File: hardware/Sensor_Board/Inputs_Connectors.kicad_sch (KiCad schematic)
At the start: 0 parts

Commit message: feat(Hw):Batt_Board_Pro_Added
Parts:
- added FLEX1: FH12-24S-0.5SH(55), Connector_FFC-FPC:Hirose_FH12-24S-0.5SH_1x24-1MP_P0.50mm_Horizontal, symbol F31L-1A7H1-11024:F31L-1A7H1-11024
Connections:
- new net +3.3V: FLEX1.1, FLEX1.2
- new net AP_ADO: FLEX1.16
- new net DIO2: FLEX1.3
- new net FSYNC: FLEX1.18
- new net GND: FLEX1.24
- new net INT1: FLEX1.17
- new net INT2: FLEX1.19
- new net R0_ANT_SW: FLEX1.13
- new net R0_BUSY: FLEX1.9
- new net R0_DIO1: FLEX1.12
- new net R0_DIO2: FLEX1.11
- new net R0_DIO3: FLEX1.10
- new net R0_MISO: FLEX1.6
- new net R0_MOSI: FLEX1.7
- new net R0_NSS: FLEX1.4
- new net R0_RST: FLEX1.8
- new net R0_SCK: FLEX1.5
- new net SCL_BME280: FLEX1.21, FLEX1.23
- new net SCL_ICM: FLEX1.15
- new net SDA_BME280: FLEX1.20, FLEX1.22
- new net SDA_ICM: FLEX1.14

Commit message: feat(Hw):Update_Battery_Sch_And_Sensors_And_PWNCube
pending_Outputs_connectors
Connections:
- net +3.3V: no longer FLEX1.2
- net SCL_BME280: no longer FLEX1.23
- net SDA_BME280: no longer FLEX1.22
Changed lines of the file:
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@@
 	(generator_version "9.0")
 	(paper "A4")
-	(junction
-		(at 115.57 52.07)
-		(diameter 0)
-		(color 0 0 0 0)
-	)
 	(wire
 		(pts
@@
 	(wire
 		(pts
-			(xy 115.57 52.07) (xy 111.76 52.07)
+			(xy 111.76 52.07) (xy 119.38 52.07)
 		)
 		(stroke
@@
 	(wire
 		(pts
-			(xy 115.57 48.26) (xy 115.57 52.07)
-		)
-		(stroke
-			(width 0)
-			(type default)
-		)
-	)
-	(wire
-		(pts
 			(xy 114.3 82.55) (xy 119.38 82.55)
 		)
@@
 	(wire
 		(pts
-			(xy 115.57 52.07) (xy 119.38 52.07)
-		)
-		(stroke
-			(width 0)
-			(type default)
-		)
-	)
-	(wire
-		(pts
 			(xy 119.38 110.49) (xy 113.03 110.49)
 		)
@@
 	(wire
 		(pts
-			(xy 115.57 54.61) (xy 115.57 52.07)
-		)
-		(stroke
-			(width 0)
-			(type default)
-		)
-	)
-	(wire
-		(pts
 			(xy 114.3 90.17) (xy 119.38 90.17)
 		)
@@
 		)
 	)
+	(hierarchical_label "R1_SCK"
+		(shape input)
+		(at 63.5 135.89 180)
+		(effects
+			(font
+				(size 1.27 1.27)
+			)
+			(justify right)
+		)
+	)
+	(hierarchical_label "R1_DIO1"
+		(shape input)
+		(at 63.5 153.67 180)
+		(effects
+			(font
+				(size 1.27 1.27)
+			)
+			(justify right)
+		)
+	)
+	(hierarchical_label "R1_MISO"
+		(shape input)
+		(at 63.5 138.43 180)
+		(effects
+			(font
+				(size 1.27 1.27)
+			)
+			(justify right)
+		)
+	)
+	(hierarchical_label "+3.3V"
+		(shape output)
+		(at 111.76 52.07 180)
+		(effects
+			(font
+				(size 1.27 1.27)
+			)
+			(justify right)
+		)
+	)
+	(hierarchical_label "INT2"
+		(shape input)
+		(at 114.3 97.79 180)
+		(effects
+			(font
+				(size 1.27 1.27)
+			)
+			(justify right)
+		)
+	)
 	(hierarchical_label "SCL_BME280"
 		(shape output)
-		(at 114.3 107.95 180)
-		(effects
-			(font
-				(size 1.27 1.27)
-			)
-			(justify right)
-		)
-	)
-	(hierarchical_label "R1_SCK"
-		(shape input)
-		(at 63.5 135.89 180)
-		(effects
-			(font
-				(size 1.27 1.27)
-			)
-			(justify right)
-		)
-	)
-	(hierarchical_label "R1_DIO1"
-		(shape input)
-		(at 63.5 153.67 180)
-		(effects
-			(font
-				(size 1.27 1.27)
-			)
-			(justify right)
-		)
-	)
-	(hierarchical_label "R1_MISO"
-		(shape input)
-		(at 63.5 138.43 180)
-		(effects
-			(font
-				(size 1.27 1.27)
-			)
-			(justify right)
-		)
-	)
-	(hierarchical_label "+3.3V"
-		(shape output)
-		(at 111.76 52.07 180)
-		(effects
-			(font
-				(size 1.27 1.27)
-			)
-			(justify right)
-		)
-	)
-	(hierarchical_label "INT2"
-		(shape input)
-		(at 114.3 97.79 180)
-		(effects
-			(font
-				(size 1.27 1.27)
-			)
-			(justify right)
-		)
-	)
-	(hierarchical_label "SCL_BME280"
-		(shape output)
 		(at 114.3 102.87 180)
 		(effects
@@
 		(shape output)
 		(at 114.3 95.25 180)
-		(effects
-			(font
-				(size 1.27 1.27)
-			)
-			(justify right)
-		)
-	)
-	(hierarchical_label "SDA_BME280"
-		(shape bidirectional)
-		(at 114.3 105.41 180)
 		(effects
 			(font
@@
 					(unit 1)
 				)
-			)
-		)
-	)
-	(symbol
-		(lib_id "power:+3.3V")
-		(at 115.57 48.26 0)
-		(unit 1)
-		(exclude_from_sim no)
-		(in_bom yes)
-		(on_board yes)
-		(dnp no)
-		(fields_autoplaced yes)
-		(property "Reference" "#PWR064"
-			(at 115.57 52.07 0)
-			(effects
-				(font
-					(size 1.27 1.27)
-				)
-				(hide yes)
-			)
-		)
-		(property "Value" "+3.3V"
-			(at 115.57 43.18 0)
-			(effects
-				(font
-					(size 1.27 1.27)
-				)
-			)
-		)
-		(property "Footprint" ""
-			(at 115.57 48.26 0)
-			(effects
-				(font
-					(size 1.27 1.27)
-				)
-				(hide yes)
-			)
-		)
-		(property "Datasheet" ""
-			(at 115.57 48.26 0)
-			(effects
-				(font
-					(size 1.27 1.27)
-				)
-				(hide yes)
-			)
-		)
-		(property "Description" "Power symbol creates a global label with name \"+3.3V\""
-			(at 115.57 48.26 0)
-			(effects
-				(font
-					(size 1.27 1.27)
-				)
-				(hide yes)
-			)
-		)
-		(pin "1"
-		)
-		(instances
-			(project "Sensor_Board"
-				(path "/671dafcd-6579-4545-95ba-aa32d81f1541/082363ca-5881-4851-9449-c4a5f2b44a24"
-					(reference "#PWR064")
-					(unit 1)
-				)

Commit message: feat(Hw):floorplans_updated
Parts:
- removed FLEX1: FH12-24S-0.5SH(55), Connector_FFC-FPC:Hirose_FH12-24S-0.5SH_1x24-1MP_P0.50mm_Horizontal, symbol F31L-1A7H1-11024:F31L-1A7H1-11024
- added J3: Sensors, Connector_PinHeader_2.54mm:PinHeader_2x20_P2.54mm_Vertical, symbol Connector_Generic:Conn_02x20_Odd_Even
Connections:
- net +3.3V: now also J3.2 (Pin_2), J3.4 (Pin_4), J3.6 (Pin_6)
- net AP_ADO: now also J3.12 (Pin_12)
- net DIO2: now also J3.1 (Pin_1)
- net DIO23: now also J3.25 (Pin_25)
- net FSYNC: now also J3.16 (Pin_16)
- net GND: now also J3.36 (Pin_36), J3.38 (Pin_38), J3.40 (Pin_40)
- net INT1: now also J3.14 (Pin_14)
- net INT2: now also J3.18 (Pin_18)
- net R0_ANT_SW: now also J3.21 (Pin_21)
- net R0_BUSY: now also J3.13 (Pin_13)
- net R0_DIO1: now also J3.19 (Pin_19)
- net R0_DIO2: now also J3.17 (Pin_17)
- net R0_DIO3: now also J3.15 (Pin_15)
- net R0_MISO: now also J3.7 (Pin_7)
- net R0_MOSI: now also J3.9 (Pin_9)
- net R0_NSS: now also J3.3 (Pin_3)
- net R0_RST: now also J3.11 (Pin_11)
- net R0_SCK: now also J3.5 (Pin_5)
- net R1_ANT_SW: now also J3.23 (Pin_23)
- net R1_BUSY: now also J3.37 (Pin_37)
- net R1_DIO1: now also J3.32 (Pin_32)
- net R1_DIO2: now also J3.34 (Pin_34)
- net R1_DIO3: now also J3.39 (Pin_39)
- net R1_MISO: now also J3.31 (Pin_31)
- net R1_MOSI: now also J3.33 (Pin_33)
- net R1_NSS: now also J3.27 (Pin_27)
- net R1_RST: now also J3.35 (Pin_35)
- net R1_SCK: now also J3.29 (Pin_29)
- net SCL_BME280: now also J3.22 (Pin_22)
- net SCL_ICM: now also J3.10 (Pin_10)
- net SDA_BME280: now also J3.20 (Pin_20)
- net SDA_ICM: now also J3.8 (Pin_8)
- no-connect marks 0 -> 4

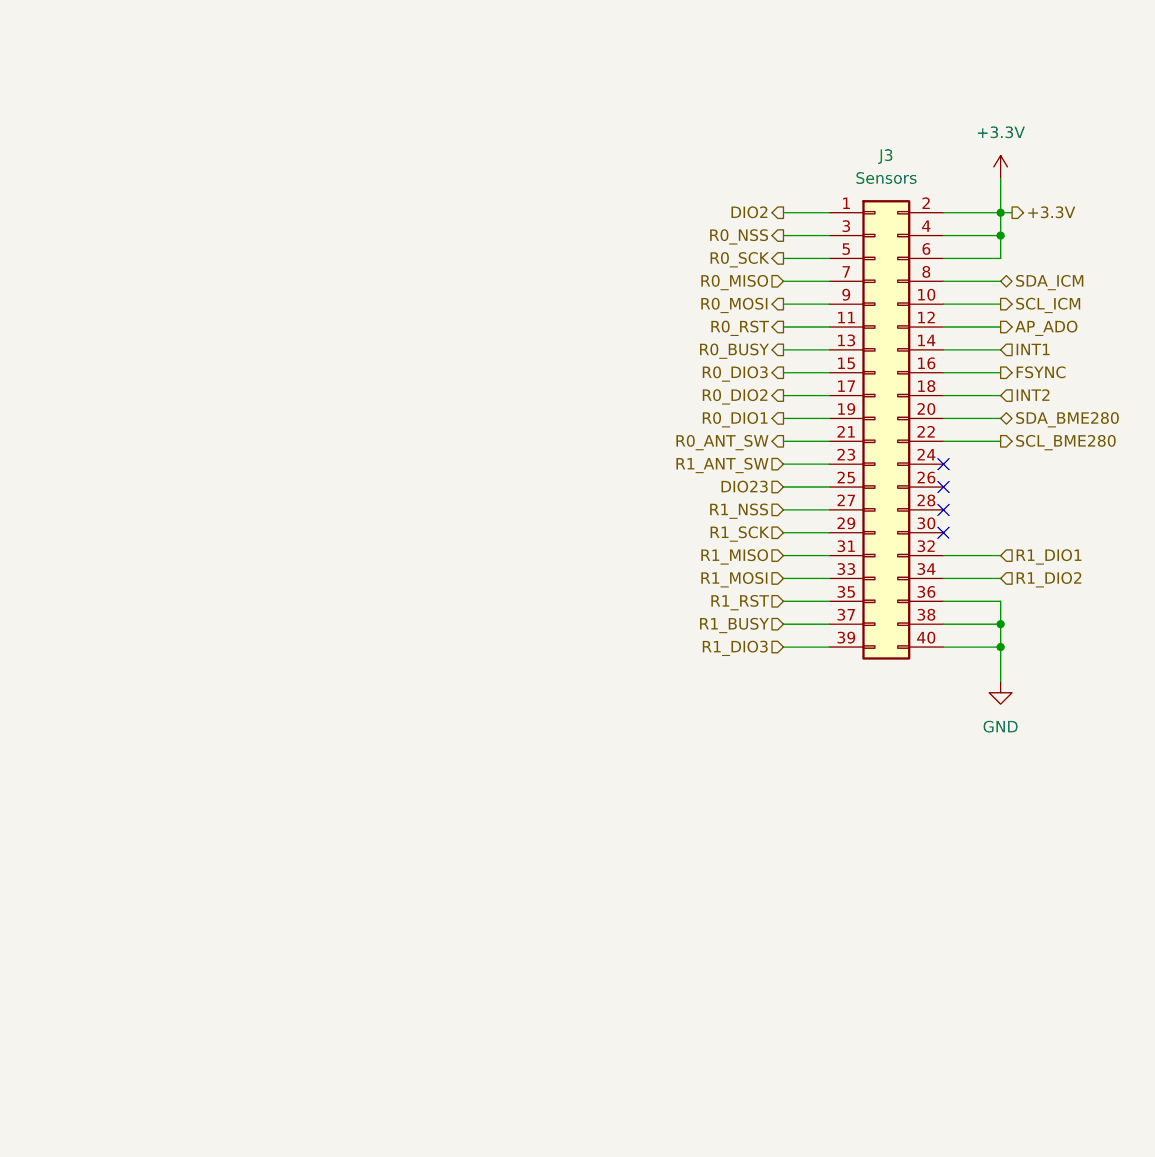
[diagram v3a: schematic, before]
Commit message: feat(Hw):Update_Route_And_3d_Model_PWNsat_Batt_Board_And_Sensors
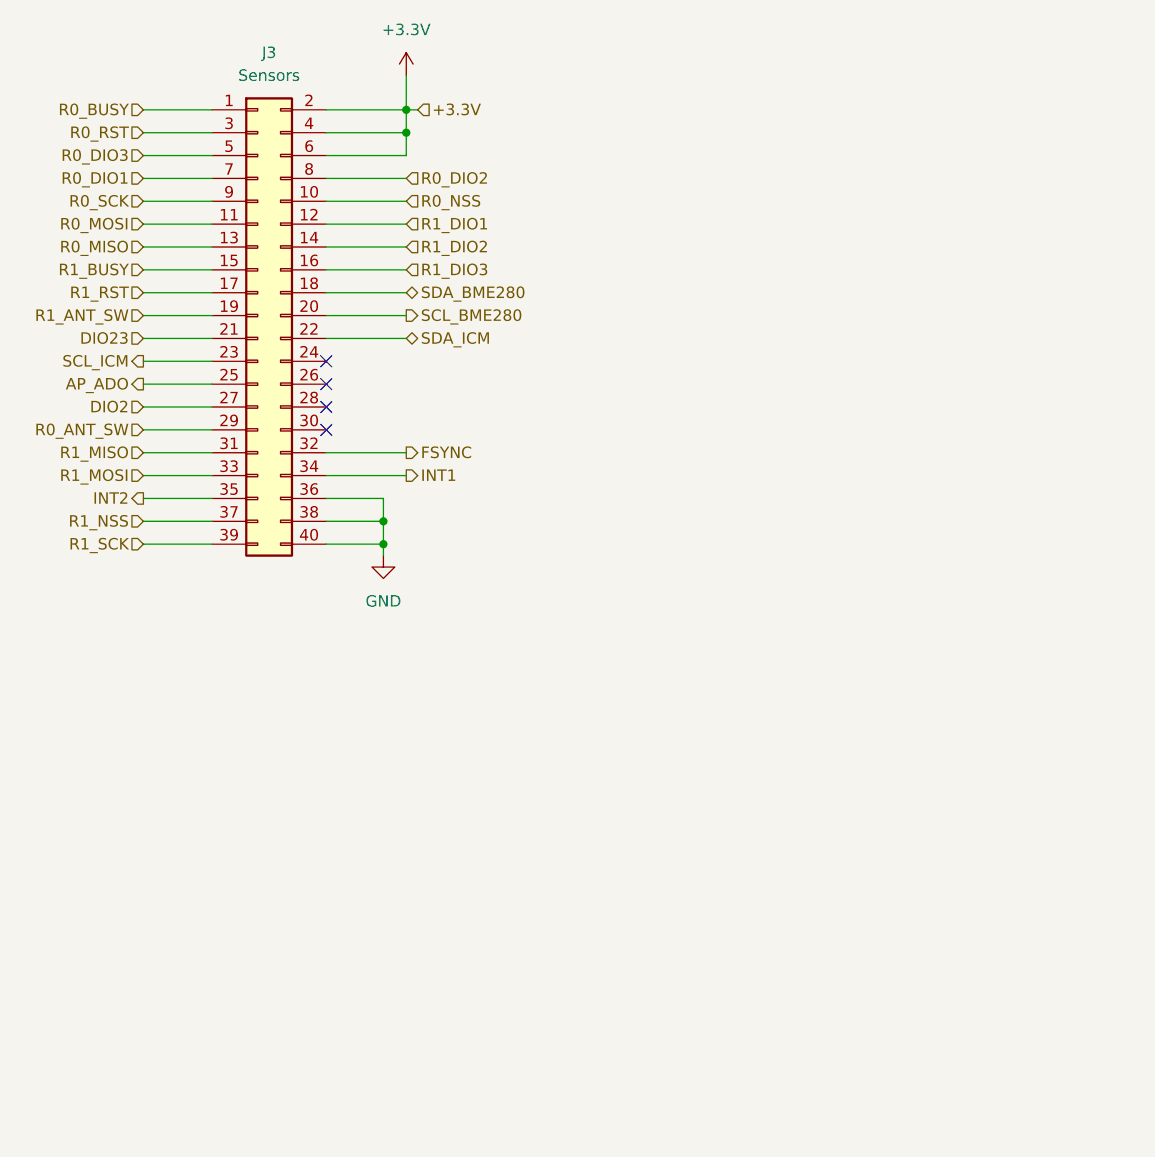
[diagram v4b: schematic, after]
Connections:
- net AP_ADO: now also J3.25 (Pin_25); no longer J3.12 (Pin_12)
- net DIO2: now also J3.27 (Pin_27); no longer J3.1 (Pin_1)
- net DIO23: now also J3.21 (Pin_21); no longer J3.25 (Pin_25)
- net FSYNC: now also J3.32 (Pin_32); no longer J3.16 (Pin_16)
- net INT1: now also J3.34 (Pin_34); no longer J3.14 (Pin_14)
- net INT2: now also J3.35 (Pin_35); no longer J3.18 (Pin_18)
- net R0_ANT_SW: now also J3.29 (Pin_29); no longer J3.21 (Pin_21)
- net R0_BUSY: now also J3.1 (Pin_1); no longer J3.13 (Pin_13)
- net R0_DIO1: now also J3.7 (Pin_7); no longer J3.19 (Pin_19)
- net R0_DIO2: now also J3.8 (Pin_8); no longer J3.17 (Pin_17)
- net R0_DIO3: now also J3.5 (Pin_5); no longer J3.15 (Pin_15)
- net R0_MISO: now also J3.13 (Pin_13); no longer J3.7 (Pin_7)
- net R0_MOSI: now also J3.11 (Pin_11); no longer J3.9 (Pin_9)
- net R0_NSS: now also J3.10 (Pin_10); no longer J3.3 (Pin_3)
- net R0_RST: now also J3.3 (Pin_3); no longer J3.11 (Pin_11)
- net R0_SCK: now also J3.9 (Pin_9); no longer J3.5 (Pin_5)
- net R1_ANT_SW: now also J3.19 (Pin_19); no longer J3.23 (Pin_23)
- net R1_BUSY: now also J3.15 (Pin_15); no longer J3.37 (Pin_37)
- net R1_DIO1: now also J3.12 (Pin_12); no longer J3.32 (Pin_32)
- net R1_DIO2: now also J3.14 (Pin_14); no longer J3.34 (Pin_34)
- net R1_DIO3: now also J3.16 (Pin_16); no longer J3.39 (Pin_39)
- net R1_NSS: now also J3.37 (Pin_37); no longer J3.27 (Pin_27)
- net R1_RST: now also J3.17 (Pin_17); no longer J3.35 (Pin_35)
- net R1_SCK: now also J3.39 (Pin_39); no longer J3.29 (Pin_29)
- net SCL_BME280: now also J3.20 (Pin_20); no longer J3.22 (Pin_22)
- net SCL_ICM: now also J3.23 (Pin_23); no longer J3.10 (Pin_10)
- net SDA_BME280: now also J3.18 (Pin_18); no longer J3.20 (Pin_20)
- net SDA_ICM: now also J3.22 (Pin_22); no longer J3.8 (Pin_8)
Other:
- moved on the sheet: J3

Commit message: fix(Hw):Tracks_modified
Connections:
- net SCL_BME280 renamed SCL_SENS
- net SCL_ICM: no longer names the net of J3.23 (Pin_23)
- net SDA_BME280 renamed SDA_SENS
- net SDA_ICM: no longer names the net of J3.22 (Pin_22)
- no-connect marks 4 -> 6
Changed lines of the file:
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@@
+	)
+	(no_connect
+		(at 73.66 66.04)
 	)
 	(no_connect
 		(at 73.66 73.66)
 	)
+	(no_connect
+		(at 53.34 68.58)
+	)
 	(wire
 		(pts
@@
 	(wire
 		(pts
-			(xy 82.55 66.04) (xy 73.66 66.04)
-		)
-		(stroke
-			(width 0)
-			(type default)
-		)
-	)
-	(wire
-		(pts
 			(xy 53.34 53.34) (xy 60.96 53.34)
 		)
@@
 			)
 			(justify right)
-		)
-	)
-	(hierarchical_label "SDA_BME280"
-		(shape bidirectional)
-		(at 82.55 60.96 0)
-		(effects
-			(font
-				(size 1.27 1.27)
-			)
-			(justify left)
-		)
-	)
-	(hierarchical_label "SCL_BME280"
-		(shape output)
-		(at 82.55 63.5 0)
-		(effects
-			(font
-				(size 1.27 1.27)
-			)
-			(justify left)
 		)
 	)
@@
 		)
 	)
+	(hierarchical_label "SDA_SENS"
+		(shape bidirectional)
+		(at 82.55 60.96 0)
+		(effects
+			(font
+				(size 1.27 1.27)
+			)
+			(justify left)
+		)
+	)
 	(hierarchical_label "R0_MISO"
 		(shape input)
@@
 		)
 	)
-	(hierarchical_label "SDA_ICM"
-		(shape bidirectional)
-		(at 82.55 66.04 0)
-		(effects
-			(font
-				(size 1.27 1.27)
-			)
-			(justify left)
-		)
-	)
 	(hierarchical_label "R0_NSS"
 		(shape input)
@@
 			)
 			(justify left)
-		)
-	)
-	(hierarchical_label "SCL_ICM"
-		(shape output)
-		(at 53.34 68.58 180)
-		(effects
-			(font
-				(size 1.27 1.27)
-			)
-			(justify right)
 		)
 	)
@@
 		)
 	)
+	(hierarchical_label "SCL_SENS"
+		(shape output)
+		(at 82.55 63.5 0)
+		(effects
+			(font
+				(size 1.27 1.27)
+			)
+			(justify left)
+		)
+	)

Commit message: feat(Hw):labels_updated
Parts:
- J3: LCSC# (none) -> C7501249
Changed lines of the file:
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@@
+			)
+		)
+		(property "LCSC#" "C7501249"
+			(at 66.04 63.5 0)
+			(effects
+				(font
+					(size 1.27 1.27)
+				)
+				(hide yes)
 			)
 		)
